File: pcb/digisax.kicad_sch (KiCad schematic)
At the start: 2 parts, among them SW1 SW_Push, U1 ESP32-S3

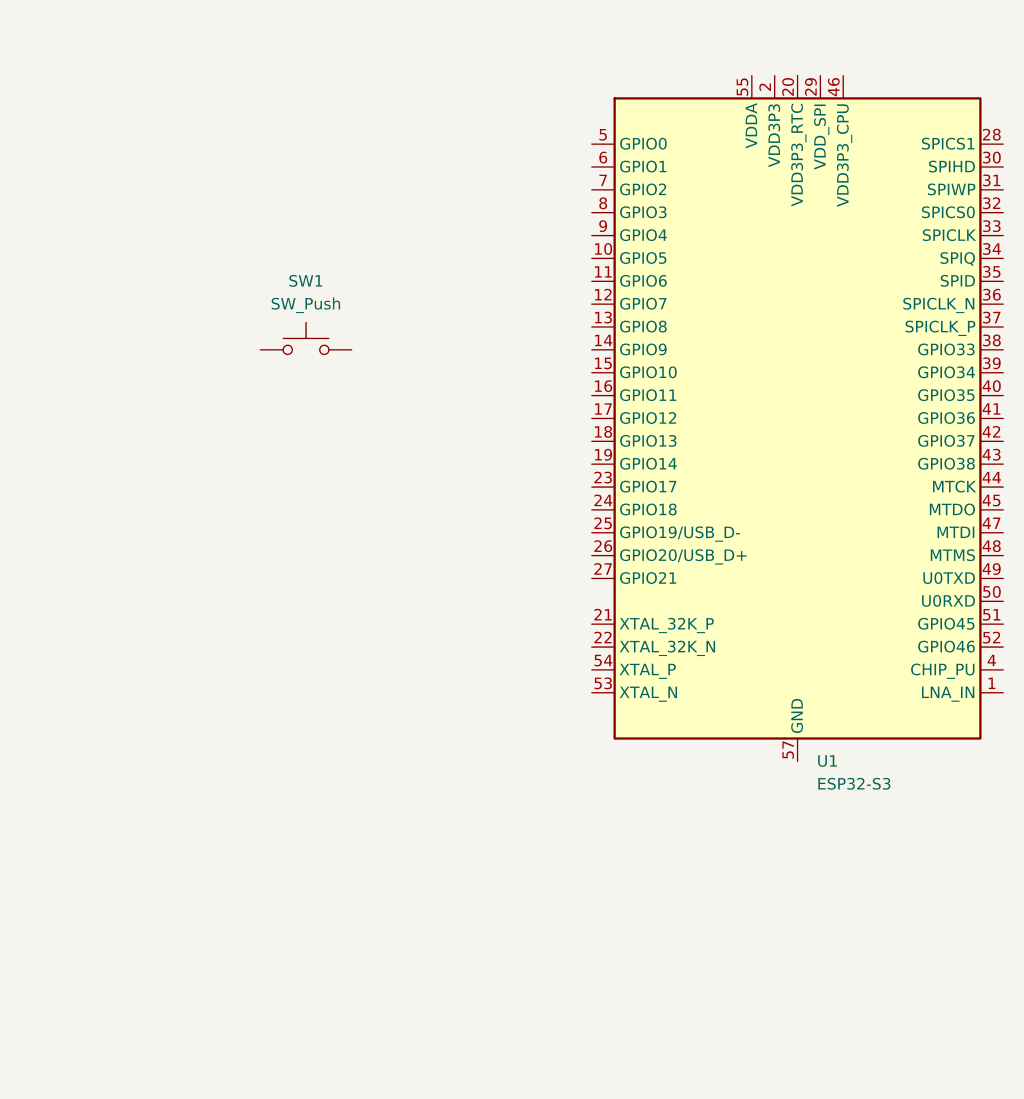
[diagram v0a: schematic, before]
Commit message: completed esp32 devboard symbol
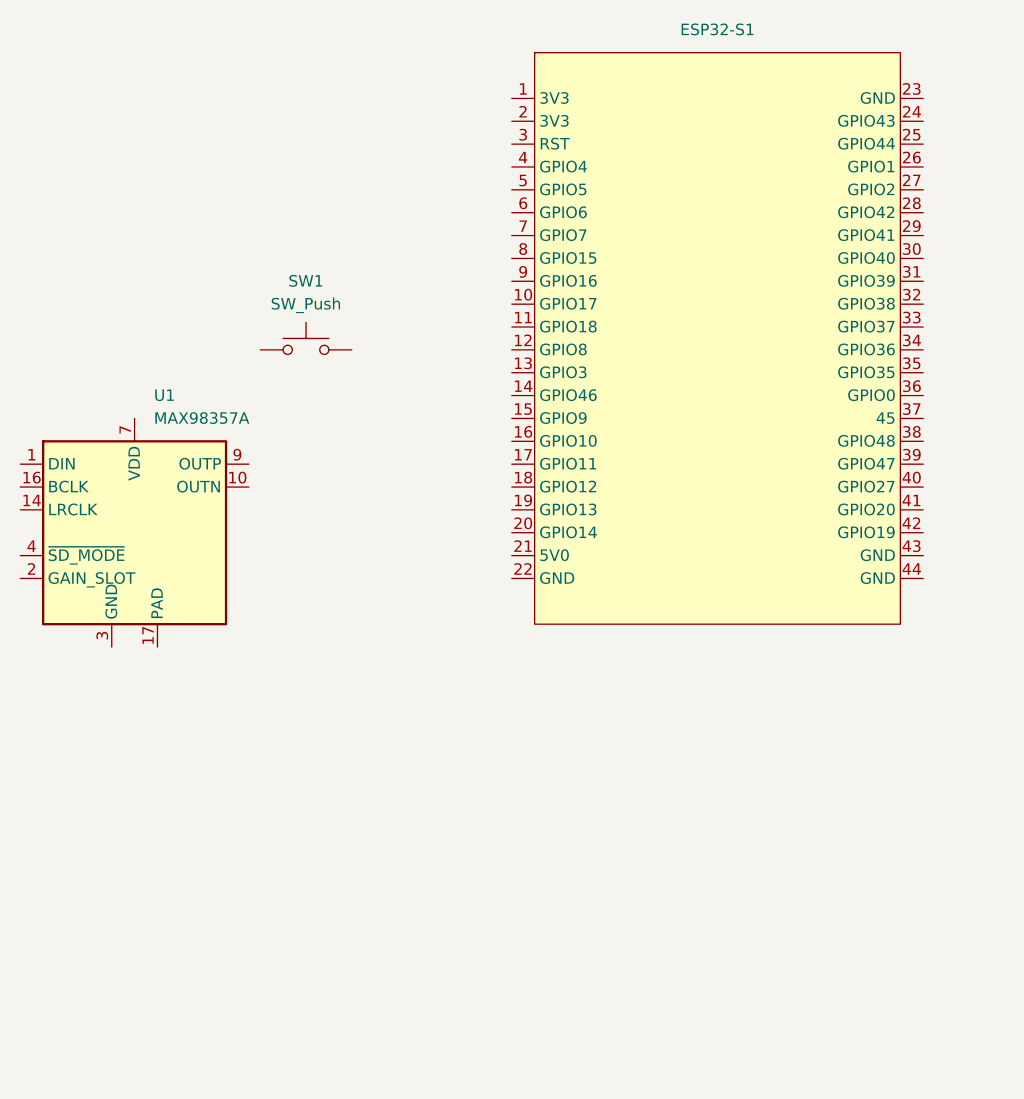
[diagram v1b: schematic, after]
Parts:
- removed U1: ESP32-S3, Package_DFN_QFN:QFN-56-1EP_7x7mm_P0.4mm_EP4x4mm, symbol MCU_Espressif:ESP32-S3
- added ESP32-S1: (no value), symbol 1_ESP32-S3-DevKitC-1:ESP32-S3-DevKitC-1
- added U1: MAX98357A, Package_DFN_QFN:TQFN-16-1EP_3x3mm_P0.5mm_EP1.23x1.23mm, symbol Audio:MAX98357A
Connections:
- new net: U1.11 (GND), U1.15 (GND), U1.3 (GND)
- new net: U1.7 (VDD), U1.8 (VDD)
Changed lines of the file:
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@@
 	(paper "A4")
 	(symbol
-		(lib_id "MCU_Espressif:ESP32-S3")
-		(at 171.45 92.71 0)
+		(lib_id "1_ESP32-S3-DevKitC-1:ESP32-S3-DevKitC-1")
+		(at 162.56 85.09 0)
 		(unit 1)
 		(body_style 1)
@@
 		(dnp no)
 		(fields_autoplaced yes)
-		(property "Reference" "U1"
-			(at 173.5933 130.81 0)
-			(show_name no)
-			(do_not_autoplace no)
-			(effects
-				(font
-					(size 1.27 1.27)
-				)
-				(justify left)
-			)
-		)
-		(property "Value" "ESP32-S3"
-			(at 173.5933 133.35 0)
-			(show_name no)
-			(do_not_autoplace no)
-			(effects
-				(font
-					(size 1.27 1.27)
-				)
-				(justify left)
-			)
-		)
-		(property "Footprint" "Package_DFN_QFN:QFN-56-1EP_7x7mm_P0.4mm_EP4x4mm"
-			(at 171.45 140.97 0)
-			(hide yes)
-			(show_name no)
-			(do_not_autoplace no)
-			(effects
-				(font
-					(size 1.27 1.27)
-				)
-			)
-		)
-		(property "Datasheet" "https://www.espressif.com/sites/default/files/documentation/esp32-s3_datasheet_en.pdf"
-			(at 171.45 92.71 0)
-			(hide yes)
-			(show_name no)
-			(do_not_autoplace no)
-			(effects
-				(font
-					(size 1.27 1.27)
-				)
-			)
-		)
-		(property "Description" "Microcontroller, Wi-Fi 802.11b/g/n, Bluetooth, 32bit"
-			(at 171.45 92.71 0)
-			(hide yes)
-			(show_name no)
-			(do_not_autoplace no)
-			(effects
-				(font
-					(size 1.27 1.27)
-				)
-			)
+		(property "Reference" "ESP32-S1"
+			(at 162.56 49.53 0)
+			(show_name no)
+			(do_not_autoplace no)
+			(effects
+				(font
+					(size 1.27 1.27)
+				)
+			)
+		)
+		(property "Value" ""
+			(at 162.56 85.09 0)
+			(show_name no)
+			(do_not_autoplace no)
+			(effects
+				(font
+					(size 1.27 1.27)
+				)
+			)
+		)
+		(property "Footprint" ""
+			(at 162.56 85.09 0)
+			(hide yes)
+			(show_name no)
+			(do_not_autoplace no)
+			(effects
+				(font
+					(size 1.27 1.27)
+				)
+			)
+		)
+		(property "Datasheet" ""
+			(at 162.56 85.09 0)
+			(hide yes)
+			(show_name no)
+			(do_not_autoplace no)
+			(effects
+				(font
+					(size 1.27 1.27)
+				)
+			)
+		)
+		(property "Description" ""
+			(at 162.56 85.09 0)
+			(hide yes)
+			(show_name no)
+			(do_not_autoplace no)
+			(effects
+				(font
+					(size 1.27 1.27)
+				)
+			)
+		)
+		(pin "19"
+		)
+		(pin "18"
+		)
+		(pin "20"
+		)
+		(pin "13"
+		)
+		(pin "12"
+		)
+		(pin "11"
+		)
+		(pin "10"
+		)
+		(pin "9"
+		)
+		(pin "8"
+		)
+		(pin "7"
+		)
+		(pin "6"
+		)
+		(pin "5"
+		)
+		(pin "4"
+		)
+		(pin "3"
 		)
 		(pin "2"
 		)
-		(pin "3"
-		)
-		(pin "20"
-		)
-		(pin "19"
-		)
-		(pin "18"
-		)
-		(pin "11"
-		)
-		(pin "10"
-		)
-		(pin "9"
-		)
-		(pin "8"
-		)
-		(pin "7"
-		)
-		(pin "13"
+		(pin "1"
+		)
+		(pin "16"
 		)
 		(pin "14"
 		)
-		(pin "16"
-		)
 		(pin "15"
 		)
-		(pin "12"
-		)
 		(pin "17"
 		)
-		(pin "4"
-		)
-		(pin "5"
-		)
-		(pin "6"
-		)
-		(pin "1"
-		)
-		(pin "56"
-		)
-		(pin "45"
-		)
-		(pin "51"
+		(pin "40"
+		)
+		(pin "41"
+		)
+		(pin "42"
+		)
+		(pin "43"
+		)
+		(pin "44"
+		)
+		(pin "32"
+		)
+		(pin "34"
+		)
+		(pin "33"
+		)
+		(pin "21"
+		)
+		(pin "37"
+		)
+		(pin "38"
+		)
+		(pin "35"
+		)
+		(pin "39"
 		)
 		(pin "36"
 		)
-		(pin "21"
+		(pin "31"
+		)
+		(pin "30"
+		)
+		(pin "29"
+		)
+		(pin "28"
+		)
+		(pin "27"
+		)
+		(pin "26"
+		)
+		(pin "25"
+		)
+		(pin "24"
+		)
+		(pin "23"
 		)
 		(pin "22"
-		)
-		(pin "23"
-		)
-		(pin "24"
-		)
-		(pin "25"
-		)
-		(pin "26"
-		)
-		(pin "27"
-		)
-		(pin "28"
-		)
-		(pin "30"
-		)
-		(pin "31"
-		)
-		(pin "33"
-		)
-		(pin "34"
-		)
-		(pin "37"
-		)
-		(pin "38"
-		)
-		(pin "40"
-		)
-		(pin "41"
-		)
-		(pin "29"
-		)
-		(pin "32"
-		)
-		(pin "35"
-		)
-		(pin "39"
-		)
-		(pin "43"
-		)
-		(pin "42"
-		)
-		(pin "47"
-		)
-		(pin "46"
-		)
-		(pin "44"
-		)
-		(pin "48"
-		)
-		(pin "49"
-		)
-		(pin "50"
-		)
-		(pin "52"
-		)
-		(pin "53"
-		)
-		(pin "54"
-		)
-		(pin "55"
-		)
-		(pin "57"
 		)
 		(instances
 			(project "digisax"
 				(path "/eb5dc4d3-8e2b-4a19-9d6b-e55e1d276974"
-					(reference "U1")
+					(reference "ESP32-S1")
 					(unit 1)
 				)
@@
 					(unit 1)
 				)
+			)
+		)
+	)
+	(symbol
+		(lib_id "Audio:MAX98357A")
+		(at 97.79 105.41 0)
+		(unit 1)
+		(body_style 1)
+		(exclude_from_sim no)
+		(in_bom yes)
+		(on_board yes)
+		(in_pos_files yes)
+		(dnp no)
+		(fields_autoplaced yes)
+		(property "Reference" "U1"
+			(at 99.9333 90.17 0)
+			(show_name no)
+			(do_not_autoplace no)
+			(effects
+				(font
+					(size 1.27 1.27)
+				)
+				(justify left)
+			)
+		)
+		(property "Value" "MAX98357A"
+			(at 99.9333 92.71 0)
+			(show_name no)
+			(do_not_autoplace no)
+			(effects
+				(font
+					(size 1.27 1.27)
+				)
+				(justify left)
+			)
+		)
+		(property "Footprint" "Package_DFN_QFN:TQFN-16-1EP_3x3mm_P0.5mm_EP1.23x1.23mm"
+			(at 96.52 107.95 0)
+			(hide yes)
+			(show_name no)
+			(do_not_autoplace no)
+			(effects
+				(font
+					(size 1.27 1.27)
+				)
+			)
+		)
+		(property "Datasheet" "https://www.analog.com/media/en/technical-documentation/data-sheets/MAX98357A-MAX98357B.pdf"
+			(at 97.79 107.95 0)
+			(hide yes)
+			(show_name no)
+			(do_not_autoplace no)
+			(effects
+				(font
+					(size 1.27 1.27)
+				)
+			)
+		)
+		(property "Description" "Mono DAC with amplifier, I2S, PCM, TDM, 32-bit, 96khz, 3.2W, TQFP-16"
+			(at 97.79 105.41 0)
+			(hide yes)
+			(show_name no)
+			(do_not_autoplace no)
+			(effects
+				(font
+					(size 1.27 1.27)
+				)
+			)
+		)
+		(pin "14"
+		)
+		(pin "13"
+		)
+		(pin "12"
+		)
+		(pin "6"
+		)
+		(pin "10"
+		)
+		(pin "1"
+		)
+		(pin "2"
+		)
+		(pin "3"
+		)
+		(pin "4"
+		)
+		(pin "5"
+		)
+		(pin "8"
+		)
+		(pin "9"
+		)
+		(pin "11"
+		)
+		(pin "15"
+		)
+		(pin "7"
+		)
+		(pin "17"
+		)
+		(pin "16"
+		)
+		(instances
+			(project "digisax"
+				(path "/eb5dc4d3-8e2b-4a19-9d6b-e55e1d276974"
+					(reference "U1")
+					(unit 1)
+				)

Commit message: drew symbols for dac and manometer
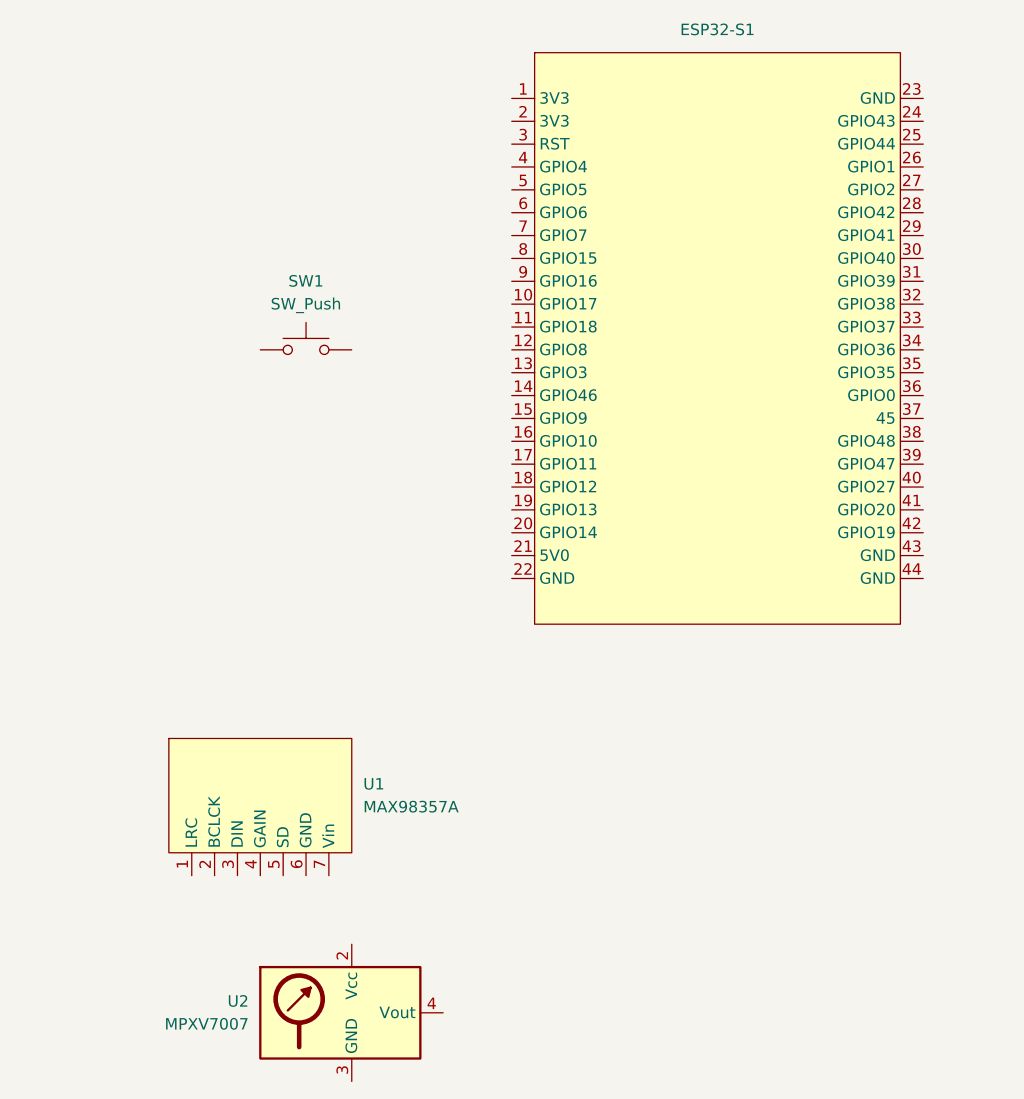
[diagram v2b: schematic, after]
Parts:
- removed U1: MAX98357A, Package_DFN_QFN:TQFN-16-1EP_3x3mm_P0.5mm_EP1.23x1.23mm, symbol Audio:MAX98357A
- added U1: MAX98357A, symbol Audio:MAX98357A_breakout
- added U2: MPXV7007, symbol Sensor_Pressure:MPXV7007
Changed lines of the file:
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@@
 	(paper "A4")
+	(symbol
+		(lib_name "MPXV7007_1")
+		(lib_id "Sensor_Pressure:MPXV7007")
+		(at 121.92 158.75 0)
+		(unit 1)
+		(body_style 1)
+		(exclude_from_sim no)
+		(in_bom yes)
+		(on_board yes)
+		(in_pos_files yes)
+		(dnp no)
+		(fields_autoplaced yes)
+		(property "Reference" "U2"
+			(at 110.49 157.4799 0)
+			(show_name no)
+			(do_not_autoplace no)
+			(effects
+				(font
+					(size 1.27 1.27)
+				)
+				(justify right)
+			)
+		)
+		(property "Value" "MPXV7007"
+			(at 110.49 160.0199 0)
+			(show_name no)
+			(do_not_autoplace no)
+			(effects
+				(font
+					(size 1.27 1.27)
+				)
+				(justify right)
+			)
+		)
+		(property "Footprint" ""
+			(at 121.92 158.75 0)
+			(hide yes)
+			(show_name no)
+			(do_not_autoplace no)
+			(effects
+				(font
+					(size 1.27 1.27)
+				)
+			)
+		)
+		(property "Datasheet" ""
+			(at 121.92 158.75 0)
+			(hide yes)
+			(show_name no)
+			(do_not_autoplace no)
+			(effects
+				(font
+					(size 1.27 1.27)
+				)
+			)
+		)
+		(property "Description" ""
+			(at 121.92 158.75 0)
+			(hide yes)
+			(show_name no)
+			(do_not_autoplace no)
+			(effects
+				(font
+					(size 1.27 1.27)
+				)
+			)
+		)
+		(pin "1"
+		)
+		(pin "2"
+		)
+		(pin "8"
+		)
+		(pin "5"
+		)
+		(pin "6"
+		)
+		(pin "4"
+		)
+		(pin "7"
+		)
+		(pin "3"
+		)
+		(instances
+			(project "digisax"
+				(path "/eb5dc4d3-8e2b-4a19-9d6b-e55e1d276974"
+					(reference "U2")
+					(unit 1)
+				)
+			)
+		)
+	)
 	(symbol
 		(lib_id "1_ESP32-S3-DevKitC-1:ESP32-S3-DevKitC-1")
@@
 				(path "/eb5dc4d3-8e2b-4a19-9d6b-e55e1d276974"
 					(reference "ESP32-S1")
+					(unit 1)
+				)
+			)
+		)
+	)
+	(symbol
+		(lib_id "Audio:MAX98357A_breakout")
+		(at 111.76 133.35 0)
+		(unit 1)
+		(body_style 1)
+		(exclude_from_sim no)
+		(in_bom yes)
+		(on_board yes)
+		(in_pos_files yes)
+		(dnp no)
+		(fields_autoplaced yes)
+		(property "Reference" "U1"
+			(at 123.19 133.3499 0)
+			(show_name no)
+			(do_not_autoplace no)
+			(effects
+				(font
+					(size 1.27 1.27)
+				)
+				(justify left)
+			)
+		)
+		(property "Value" "MAX98357A"
+			(at 123.19 135.8899 0)
+			(show_name no)
+			(do_not_autoplace no)
+			(effects
+				(font
+					(size 1.27 1.27)
+				)
+				(justify left)
+			)
+		)
+		(property "Footprint" ""
+			(at 111.76 133.35 0)
+			(hide yes)
+			(show_name no)
+			(do_not_autoplace no)
+			(effects
+				(font
+					(size 1.27 1.27)
+				)
+			)
+		)
+		(property "Datasheet" ""
+			(at 111.76 133.35 0)
+			(hide yes)
+			(show_name no)
+			(do_not_autoplace no)
+			(effects
+				(font
+					(size 1.27 1.27)
+				)
+			)
+		)
+		(property "Description" ""
+			(at 111.76 133.35 0)
+			(hide yes)
+			(show_name no)
+			(do_not_autoplace no)
+			(effects
+				(font
+					(size 1.27 1.27)
+				)
+			)
+		)
+		(pin "7"
+		)
+		(pin "1"
+		)
+		(pin "2"
+		)
+		(pin "4"
+		)
+		(pin "3"
+		)
+		(pin "5"
+		)
+		(pin "6"
+		)
+		(instances
+			(project "digisax"
+				(path "/eb5dc4d3-8e2b-4a19-9d6b-e55e1d276974"
+					(reference "U1")
 					(unit 1)
 				)
@@
 					(unit 1)
 				)
-			)
-		)
-	)
-	(symbol
-		(lib_id "Audio:MAX98357A")
-		(at 97.79 105.41 0)
-		(unit 1)
-		(body_style 1)
-		(exclude_from_sim no)
-		(in_bom yes)
-		(on_board yes)
-		(in_pos_files yes)
-		(dnp no)
-		(fields_autoplaced yes)
-		(property "Reference" "U1"
-			(at 99.9333 90.17 0)
-			(show_name no)
-			(do_not_autoplace no)
-			(effects
-				(font
-					(size 1.27 1.27)
-				)
-				(justify left)
-			)
-		)
-		(property "Value" "MAX98357A"
-			(at 99.9333 92.71 0)
-			(show_name no)
-			(do_not_autoplace no)
-			(effects
-				(font
-					(size 1.27 1.27)
-				)
-				(justify left)
-			)
-		)
-		(property "Footprint" "Package_DFN_QFN:TQFN-16-1EP_3x3mm_P0.5mm_EP1.23x1.23mm"
-			(at 96.52 107.95 0)
-			(hide yes)
-			(show_name no)
-			(do_not_autoplace no)
-			(effects
-				(font
-					(size 1.27 1.27)
-				)
-			)
-		)
-		(property "Datasheet" "https://www.analog.com/media/en/technical-documentation/data-sheets/MAX98357A-MAX98357B.pdf"
-			(at 97.79 107.95 0)
-			(hide yes)
-			(show_name no)
-			(do_not_autoplace no)
-			(effects
-				(font
-					(size 1.27 1.27)
-				)
-			)
-		)
-		(property "Description" "Mono DAC with amplifier, I2S, PCM, TDM, 32-bit, 96khz, 3.2W, TQFP-16"
-			(at 97.79 105.41 0)
-			(hide yes)
-			(show_name no)
-			(do_not_autoplace no)
-			(effects
-				(font
-					(size 1.27 1.27)
-				)
-			)
-		)
-		(pin "14"
-		)
-		(pin "13"
-		)
-		(pin "12"
-		)
-		(pin "6"
-		)
-		(pin "10"
-		)
-		(pin "1"
-		)
-		(pin "2"
-		)
-		(pin "3"
-		)
-		(pin "4"
-		)
-		(pin "5"
-		)
-		(pin "8"
-		)
-		(pin "9"
-		)
-		(pin "11"
-		)
-		(pin "15"
-		)
-		(pin "7"
-		)
-		(pin "17"
-		)
-		(pin "16"
-		)
-		(instances
-			(project "digisax"
-				(path "/eb5dc4d3-8e2b-4a19-9d6b-e55e1d276974"
-					(reference "U1")
-					(unit 1)
-				)
